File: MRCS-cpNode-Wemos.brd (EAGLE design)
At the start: 99.8 x 68.8 mm, 40 parts, among them CON1 3.5MM, CON2 3.5MM, J2 CONNECTOR-GROVE-4P-2.0-347013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, Q2 2n7002, Q3 2n7002, Q4 2n7002, Q5 2n7002, U3 NE555P, U4 MAX3465CPD

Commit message: 5.0
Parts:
- removed C4: 0.1uF, SPCoast:0805-CAP
- removed C6: .01uF, SPCoast:0805-CAP
- removed C7: .1uF, SPCoast:0805-CAP
- removed C8: .1uF, SPCoast:0603-CAP
- removed CON1, CON2: 3.5MM, SPCoast:SCREWTERMINAL-5MM-3
- removed CON3, CON4: (no value), SPCoast:SCREWTERMINAL-5MM-2
- removed D1: BAV-199, SPCoast:SOT23
- removed R14: 1k0, SPCoast:0805-RES
- removed RS485IN: (no value), SparkFun:1X05
- removed RS485OUT: (no value), SparkFun:1X05_LOCK
- removed TX: TX, SPCoast:0603-LED
- removed U3: NE555P, SparkFun:DIL-08
- removed U4: MAX3465CPD, maxim:DIL14
- added CMRI-IO: (no value), SPCoast:1X05_LOCK_LONGPADS
- added Q1: 2n7002, SPCoast:SOT23
- added R4: 10k, SPCoast:0805-RES
- BOARD: device SPCoast:BOARD-DINRAIL-2.7IN -> SPCoast:BOARD-DINRAIL-2.7IN-9CM
- C2, C3: device SPCoast:0805-CAP@1 -> SPCoast:0805-CAP
- R1: value (none) -> 10k; device SPCoast:1/6W-RES -> SPCoast:0805-RES
- moved Q2 17.6 mm to (54.6, 45.7)
- moved Q3 17.6 mm to (49.5, 45.7)
- moved Q4 17.6 mm to (39.4, 45.7)
- moved Q5 17.6 mm to (44.5, 45.7)
- moved R10 17.6 mm to (44.5, 50.8)
- moved R2 17.6 mm to (54.6, 41.3)
- moved R3 17.6 mm to (54.6, 50.8)
- moved R5 17.6 mm to (49.5, 41.3)
- moved R6 17.6 mm to (49.5, 50.8)
- moved R7 17.6 mm to (39.4, 41.3)
- moved R9 17.6 mm to (44.5, 41.3)
- moved R8 17.6 mm to (39.4, 50.8)
- moved R1 12.5 mm to (63.5, 41.3)
- moved CON5 11.4 mm to (76.2, 33.0)
- moved I2C 11.4 mm to (80.0, 22.9)
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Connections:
- removed net IN+: CON3.2, CON4.2, RS485IN.1, RS485OUT.1, U4.12
- removed net IN-: CON3.1, CON4.1, RS485IN.2, RS485OUT.2, U4.11
- removed net N$1: C4.1, D1.1, D1.3, R1.1, U3.6, U3.7
- removed net N$29: R14.2, TX.A
- removed net N$38: C6.1, U3.5
- removed net OUT+: CON1.3, CON2.3, RS485IN.3, RS485OUT.3, U4.9
- removed net OUT-: CON1.2, CON2.2, RS485IN.4, RS485OUT.4, U4.10
- removed net SHIELD: CON1.1, CON2.1, RS485IN.5, RS485OUT.5
- new net VCC: CMRI-IO.2
- net +3V3: now also Q1.1, R1.2
- net D5: now also Q1.2, R1.1
- net GND: now also CMRI-IO.1; no longer C4.2, C6.2, C7.2, C8.2, TX.C, U3.1, U4.6, U4.7
- net RXH: now also CMRI-IO.4; no longer U4.2
- net TXEN: now also CMRI-IO.5, Q1.3, R4.1; no longer R14.1, U3.3, U4.3, U4.4
- net TXH: now also CMRI-IO.3; no longer D1.2, U3.2, U4.5
- net VCCIO: now also R4.2; no longer C7.1, C8.1, R1.2, U3.4, U3.8, U4.14
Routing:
- net IN+: track 96.5 -> 0.00 mm, vias 1 -> 0
- net IN-: track 89.0 -> 0.00 mm, vias 2 -> 0
- net OUT+: track 82.1 -> 0.00 mm, vias 2 -> 0
- net OUT-: track 78.2 -> 0.00 mm, vias 2 -> 0
- net TXEN: track 25.3 -> 93.9 mm, vias 0 -> 3
- net SHIELD: track 51.9 -> 0.00 mm
- net RXH: track 30.5 -> 78.3 mm, vias 1 -> 4
- net D5: track 0.00 -> 33.3 mm, vias 0 -> 1
- net +3V3: track 48.4 -> 74.5 mm, vias 4 -> 5
- net N$1: track 20.4 -> 0.00 mm
- net GND: track 30.4 -> 12.0 mm, vias 24 -> 22
- net VCCIO: track 76.3 -> 92.3 mm, vias 4 -> 5
- net TX: track 24.6 -> 39.8 mm
- net SDA: track 32.2 -> 47.4 mm
- net RX: track 27.1 -> 42.4 mm
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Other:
- board size 99.8 x 68.8 mm -> 89.8 x 68.8 mm
- board text removed: "4-wire"
- board text removed: "AutoRTS"
- board text removed: "C/MRI Interface"
- board text removed: "IN"
- board text removed: "IN+"
- board text removed: "IN-"
- board text removed: "OUT"
- board text removed: "Out+"
- board text removed: "Out-"
- board text removed: "RS-485"
- board text removed: "RX"
- board text removed: "Shield"
- board text removed: "TX"

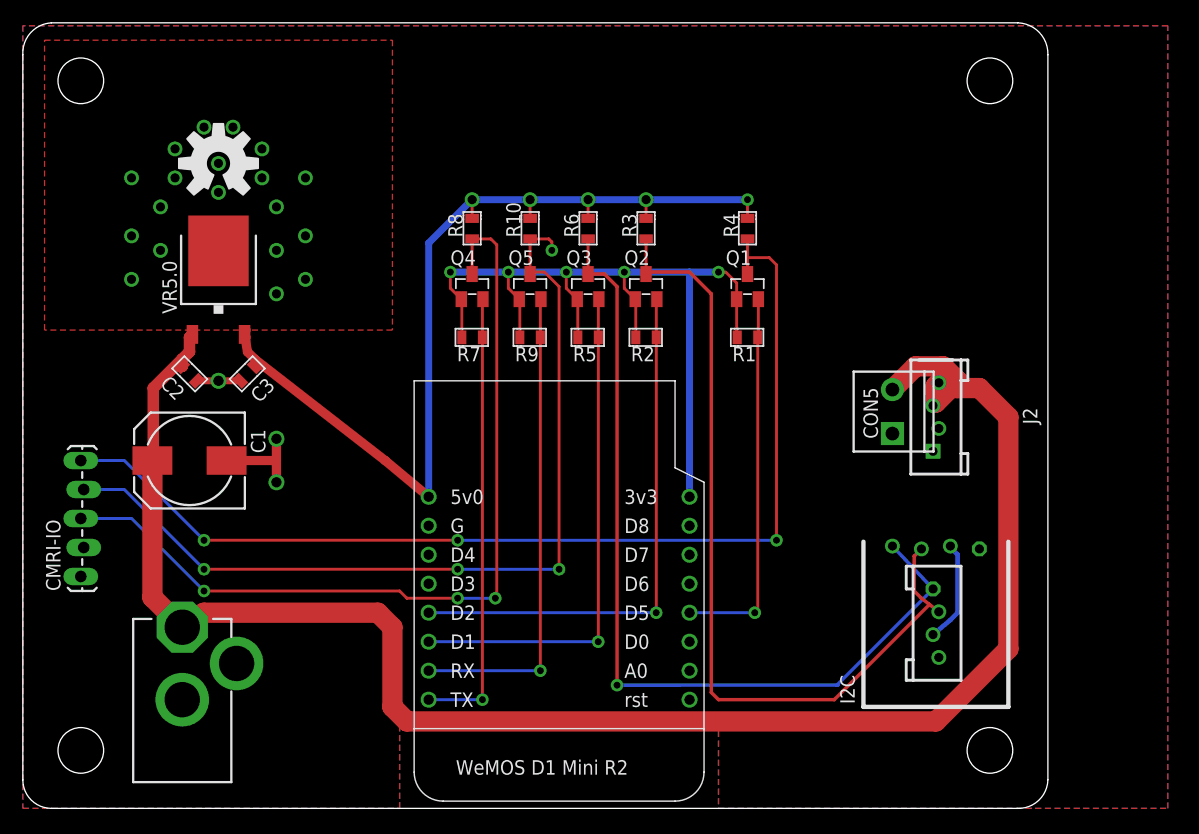
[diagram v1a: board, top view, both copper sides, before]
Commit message: cleanup, DRC, ERC
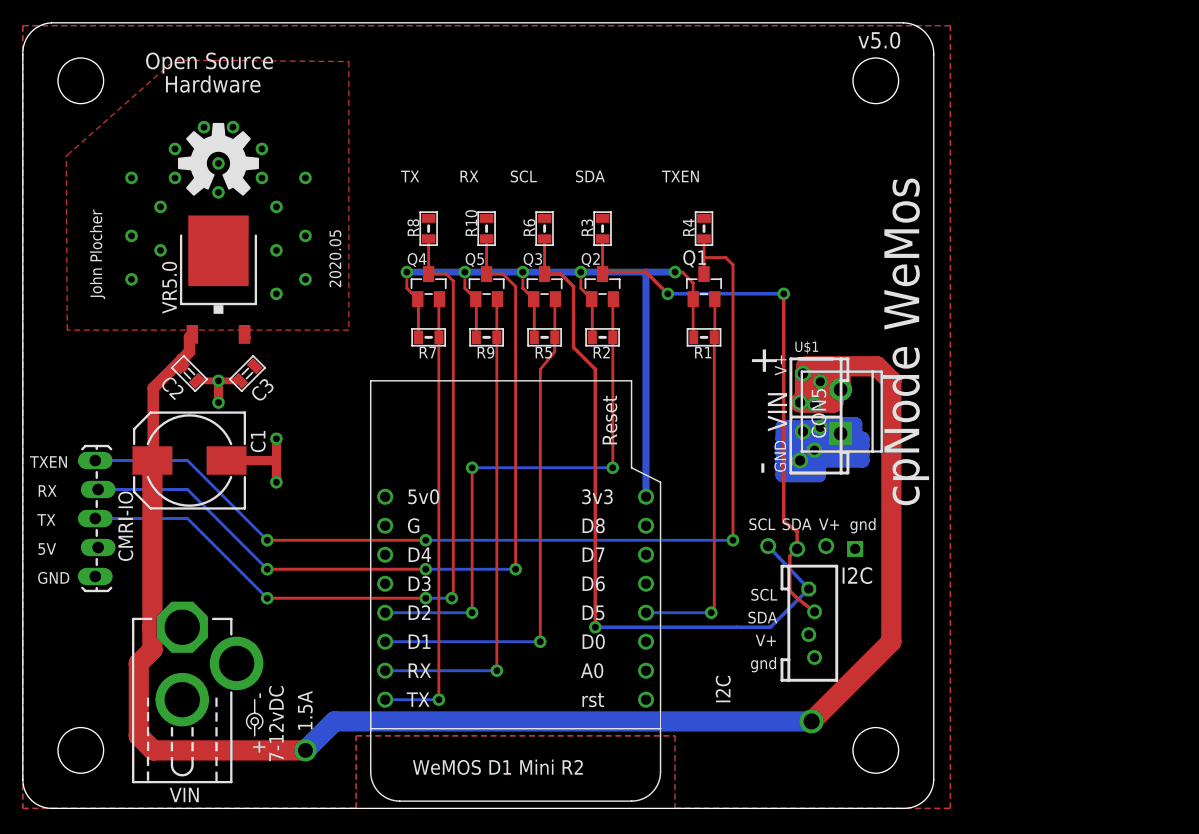
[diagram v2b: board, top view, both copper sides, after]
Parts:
- removed J2: CONNECTOR-GROVE-4P-2.0-3470130P1, SPCoast:4P-2.0
- added U$1: CONNECTOR-POWER-L, SPCoast:POWER-R2
- BOARD: device SPCoast:BOARD-DINRAIL-2.7IN-9CM -> SPCoast:BOARD-DINRAIL-2.7IN-8CM
- LABEL1: device SPCoast-minimal:POWER_USAGE -> SPCoast:PWR_LABEL
- moved LABEL1 14.5 mm to (20.3, 7.62), turned to 180 degrees
- moved I2C 10.9 mm to (69.1, 22.9)
- moved CON5 4.54 mm to (71.7, 33.0)
- moved Q1 3.81 mm to (59.7, 45.7)
- moved Q2 3.81 mm to (50.8, 45.7)
- moved Q3 3.81 mm to (45.7, 45.7)
- moved Q5 3.81 mm to (40.6, 45.7)
- moved R1 3.81 mm to (59.7, 41.3)
- moved R10 3.81 mm to (40.6, 50.8)
- moved R2 3.81 mm to (50.8, 41.3)
- moved R3 3.81 mm to (50.8, 50.8)
- moved R4 3.81 mm to (59.7, 50.8)
- moved R5 3.81 mm to (45.7, 41.3)
- moved R6 3.81 mm to (45.7, 50.8)
- moved R9 3.81 mm to (40.6, 41.3)
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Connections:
- removed net VCC: CMRI-IO.2
- net +9V: now also U$1.V+, U$1.V+@1, U$1.V+@2, U$1.V+@3; no longer J2.3, J2.4
- net GND: now also U$1.GND, U$1.GND@1, U$1.GND@2, U$1.GND@3; no longer J2.1, J2.2
- net VCCIO: now also CMRI-IO.2
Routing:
- net VCCIO: track 92.3 -> 0.82 mm, vias 5 -> 0
- net GND: track 12.0 -> 62.2 mm, vias 22 -> 23
- net SDAH: track 74.2 -> 49.5 mm, vias 0 -> 2
- net SCLH: track 77.6 -> 62.0 mm
- net +9V: track 153.6 -> 162.3 mm, vias 0 -> 2
- net TXH: track 75.7 -> 67.4 mm
- net RXH: track 78.3 -> 70.3 mm, vias 4 -> 3
- net TXEN: track 93.9 -> 88.8 mm
- net SCL: track 44.9 -> 44.1 mm
- net SDA: vias 1 -> 3
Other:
- board size 89.8 x 68.8 mm -> 79.8 x 68.8 mm
- board text added: "2020.05"
- board text added: "5V"
- board text added: "GND"
- board text added: "RX"
- board text added: "SCL"
- board text added: "SDA"
- board text added: "TX"
- board text added: "TXEN"
- board text added: "v5.0"
- board text removed: "2019.03"
- board text removed: "v4.0"

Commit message: added missing values
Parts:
- CMRI-IO: value (none) -> 0.100
- CON5: value (none) -> 3.5mm
- J1: value (none) -> 2.1mm
- U$1: value CONNECTOR-POWER-L -> I2C
- moved CON5 51.9 mm to (24.1, 12.2), turned to 0 degrees
- moved LABEL1 16.1 mm to (5.08, 12.7)
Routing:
- net GND: track 62.2 -> 13.9 mm
- net +9V: track 162.3 -> 165.6 mm
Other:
- board text added: "GND V+"
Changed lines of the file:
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@@
 <setting verticaltext="up"/>
 </settings>
-<grid distance="50" unitdist="mil" unit="mil" style="dots" multiple="2" display="yes" altdistance="5" altunitdist="mil" altunit="mil"/>
+<grid distance="50" unitdist="mil" unit="mil" style="dots" multiple="2" display="yes" altdistance="25" altunitdist="mil" altunit="mil"/>
 <layers>
 <layer number="1" name="Top" color="4" fill="1" visible="yes" active="yes"/>
@@
 <wire x1="49.673" y1="-1.905" x2="56.023" y2="2.032" width="2.54" layer="52"/>
 <text x="12.85875" y="0.53975" size="1.27" layer="21">VIN</text>
-<text x="25.38095" y="6.7216" size="1.27" layer="21" ratio="10" rot="SR90">1.5A</text>
+<text x="3.79095" y="10.5316" size="1.27" layer="21" ratio="10" rot="SR90">1.5A</text>
 <text x="78.542971875" y="26.35435625" size="3.048" layer="21" ratio="15" rot="SR90">cpNode WeMos</text>
 <wire x1="55.388" y1="-0.381" x2="26.559" y2="70.612" width="1.778" layer="52"/>
@@
 <text x="1.27" y="22.225" size="1.016" layer="21" font="vector" ratio="10">5V</text>
 <text x="1.27" y="19.685" size="1.016" layer="21" font="vector" ratio="10">GND</text>
+<text x="22.86" y="16.51" size="1.016" layer="21" font="vector" ratio="10">GND  V+</text>
+<text x="22.86" y="6.985" size="1.016" layer="21" font="vector" ratio="10">GND  V+</text>
+<text x="24.765" y="9.525" size="1.016" layer="21" font="vector" ratio="10">VIN</text>
+<text x="24.28875" y="0.53975" size="1.27" layer="21">VIN</text>
 </plain>
 <attributes>
@@
 <attribute name="NAME" x="62.008" y="9.144" size="1.27" layer="25" font="vector" ratio="11" rot="R90"/>
 </element>
-<element name="J1" library="SPCoast" package="DCJ0202" value="" x="13.97" y="12.7" smashed="yes"/>
-<element name="LABEL1" library="SPCoast" package="PWR_LABEL" value="7-12vDC" x="20.32" y="7.62" smashed="yes" rot="R180">
-<attribute name="VALUE" x="21.59" y="10.795" size="1.27" layer="21" rot="R270"/>
+<element name="J1" library="SPCoast" package="DCJ0202" value="2.1mm" x="13.97" y="12.7" smashed="yes"/>
+<element name="LABEL1" library="SPCoast" package="PWR_LABEL" value="7-12vDC" x="5.08" y="12.7" smashed="yes" rot="R180">
+<attribute name="VALUE" x="6.35" y="15.875" size="1.27" layer="21" rot="R270"/>
 </element>
 <element name="BOARD" library="SPCoast" package="BOARD-DINRAIL-2.7IN-8CM" value="BOARD80X150" x="0" y="0" smashed="yes"/>
@@
 <attribute name="VALUE" x="41.783" y="53.721" size="1.016" layer="27" rot="R180"/>
 </element>
-<element name="CON5" library="SPCoast" package="SCREWTERMINAL-3.5MM-2_LOCK" value="" x="71.66" y="33.02" smashed="yes" rot="R90">
-<attribute name="NAME" x="70.39" y="32.385" size="1.27" layer="25" rot="R90"/>
-<attribute name="VALUE" x="70.39" y="31.75" size="0.4064" layer="27" rot="R90"/>
-</element>
-<element name="CMRI-IO" library="SPCoast" package="1X05_LOCK_LONGPADS" value="" x="6.35" y="20.32" smashed="yes" rot="R90">
+<element name="CON5" library="SPCoast" package="SCREWTERMINAL-3.5MM-2_LOCK" value="3.5mm" x="24.13" y="12.16" smashed="yes">
+<attribute name="NAME" x="23.495" y="13.43" size="1.27" layer="25"/>
+<attribute name="VALUE" x="22.86" y="13.43" size="0.4064" layer="27"/>
+</element>
+<element name="CMRI-IO" library="SPCoast" package="1X05_LOCK_LONGPADS" value="0.100" x="6.35" y="20.32" smashed="yes" rot="R90">
 <attribute name="NAME" x="9.652" y="21.59" size="1.27" layer="25" font="vector" rot="R90"/>
 <attribute name="VALUE" x="9.652" y="19.05" size="1.27" layer="27" font="vector" rot="R90"/>
@@
 <attribute name="VALUE" x="60.833" y="53.721" size="1.016" layer="27" rot="R180"/>
 </element>
-<element name="U$1" library="SPCoast" package="POWER-R2" value="CONNECTOR-POWER-L" x="69.12" y="34.29" smashed="yes">
+<element name="U$1" library="SPCoast" package="POWER-R2" value="I2C" x="69.12" y="34.29" smashed="yes">
 <attribute name="NAME" x="67.596" y="40.005" size="0.889" layer="25" font="vector" ratio="11"/>
 <attribute name="VALUE" x="63.532" y="27.178" size="0.635" layer="27" font="vector" ratio="10"/>
@@
 <contactref element="U$1" pad="GND@1"/>
 <contactref element="U$1" pad="GND@3"/>
-<wire x1="71.66" y1="32.8422" x2="71.66" y2="33.02" width="1.27" layer="16"/>
-<wire x1="71.66" y1="33.02" x2="71.66" y2="33.386" width="1.27" layer="16"/>
-<wire x1="71.66" y1="33.386" x2="69.882" y2="33.386" width="1.27" layer="16"/>
-<wire x1="69.882" y1="33.386" x2="66.58" y2="33.386" width="1.27" layer="16"/>
-<wire x1="66.58" y1="33.386" x2="66.58" y2="32.385" width="1.27" layer="16"/>
-<wire x1="66.58" y1="32.385" x2="73.565" y2="32.385" width="1.27" layer="16"/>
-<wire x1="73.565" y1="32.385" x2="73.565" y2="31.75" width="1.27" layer="16"/>
-<wire x1="73.565" y1="31.75" x2="66.58" y2="31.75" width="1.27" layer="16"/>
-<wire x1="66.58" y1="31.75" x2="66.58" y2="31.115" width="1.27" layer="16"/>
-<wire x1="66.58" y1="31.115" x2="73.565" y2="31.115" width="1.27" layer="16"/>
-<wire x1="73.565" y1="31.115" x2="73.565" y2="30.48" width="1.27" layer="16"/>
-<wire x1="73.565" y1="30.48" x2="68.104" y2="30.48" width="1.27" layer="16"/>
-<wire x1="68.104" y1="30.48" x2="66.58" y2="30.48" width="1.27" layer="16"/>
-<wire x1="66.58" y1="30.48" x2="66.58" y2="29.21" width="1.27" layer="16"/>
-<wire x1="66.58" y1="29.21" x2="69.755" y2="29.21" width="1.27" layer="16"/>
-<wire x1="69.755" y1="29.21" x2="69.755" y2="30.48" width="1.27" layer="16"/>
-<wire x1="69.755" y1="30.48" x2="68.104" y2="30.48" width="1.27" layer="16"/>
-<wire x1="71.66" y1="33.02" x2="72.93" y2="33.02" width="1.27" layer="16"/>
-<wire x1="72.93" y1="33.02" x2="72.93" y2="33.655" width="1.27" layer="16"/>
-<wire x1="72.93" y1="33.655" x2="70.39" y2="33.655" width="1.27" layer="16"/>
 <via x="17.145" y="35.56" extent="1-16" drill="0.6"/>
 <wire x1="17.145" y1="35.56" x2="17.145" y2="37.465" width="0.8128" layer="1"/>
+<polygon width="0.4064" layer="16" thermals="no">
+<vertex x="66.675" y="34.29"/>
+<vertex x="71.12" y="34.29"/>
+<vertex x="71.12" y="29.21"/>
+<vertex x="66.675" y="29.21"/>
+</polygon>
 </signal>
 <signal name="+9V" class="3">
@@
 <wire x1="11.43" y1="5.08" x2="24.765" y2="5.08" width="1.778" layer="1"/>
 <wire x1="24.765" y1="5.08" x2="27.305" y2="7.62" width="1.778" layer="16"/>
-<wire x1="71.66" y1="36.6978" x2="71.66" y2="38.1" width="1.778" layer="1"/>
 <wire x1="71.66" y1="38.1" x2="69.755" y2="38.1" width="1.778" layer="1"/>
 <wire x1="69.755" y1="38.1" x2="69.755" y2="36.83" width="1.778" layer="1"/>
@@
 <via x="69.12" y="7.62" extent="1-16" drill="1.4"/>
 <via x="24.765" y="5.08" extent="1-16" drill="1.3"/>
+<wire x1="27.305" y1="7.62" x2="27.305" y2="11.6572" width="1.6764" layer="16"/>
+<wire x1="27.305" y1="11.6572" x2="27.8078" y2="12.16" width="1.6764" layer="16"/>
 </signal>
 <signal name="SDA" class="2">

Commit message: normalized values
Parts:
- BOARD: value BOARD80X150 -> BOARD
- C1: value 150uF -> 220uF
- C2, C3: device SPCoast:0805-CAP -> SPCoast:0603-CAP
- OSHW1: value OSHW-LOGOL -> OSHW
- R10, R2, R3, R4, R5, R6, R7, R8, R9: device SPCoast:0805-RES -> SPCoast:0603-RES
- VR5.0: value 5v -> CJ7805
- WEMOS: value D1Mini -> Mini-R2
- moved U$1 2.54 mm to (71.7, 34.3)
- moved VR5.0 1.27 mm to (17.1, 47.6), turned to 90 degrees
- turned Q1 to 270 degrees
- turned Q2 to 270 degrees
- turned Q3 to 270 degrees
- turned Q4 to 270 degrees
- turned Q5 to 270 degrees
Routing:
- net +9V: track 165.6 -> 175.4 mm
- net VCCIO: track 0.82 -> 2.47 mm
